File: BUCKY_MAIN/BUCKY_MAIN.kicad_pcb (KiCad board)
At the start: 2 copper layers, 156.4 x 156.4 mm, 43 parts, among them IC1 TSSP96038TR, IC10 TSSP96038TR, IC11 TSSP96038TR, IC12 TSSP96038TR, IC2 TSSP96038TR, IC3 TSSP96038TR, IC4 TSSP96038TR, IC5 TSSP96038TR, IC6 TSSP96038TR, IC7 TSSP96038TR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

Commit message: finish up robot (i think)
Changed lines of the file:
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@@
 		(model "${KICAD8_3DMODEL_DIR}/Connector_PinHeader_2.54mm.3dshapes/PinHeader_1x06_P2.54mm_Horizontal.wrl"
 			(offset
-				(xyz 0 0 0)
+				(xyz 0 -12.75 -2)
 			)
 			(scale
@@
 			)
 			(rotate
-				(xyz 0 0 0)
+				(xyz 180 0 0)
 			)
 		)
@@
 		)
 	)
+	(gr_text "MAIN -> LIGHT\n"
+		(at 167.5638 140.9192 90)
+		(layer "F.SilkS")
+		(effects
+			(font
+				(size 1.5 1.5)
+				(thickness 0.3)
+				(bold yes)
+			)
+			(justify left bottom)
+		)
+	)

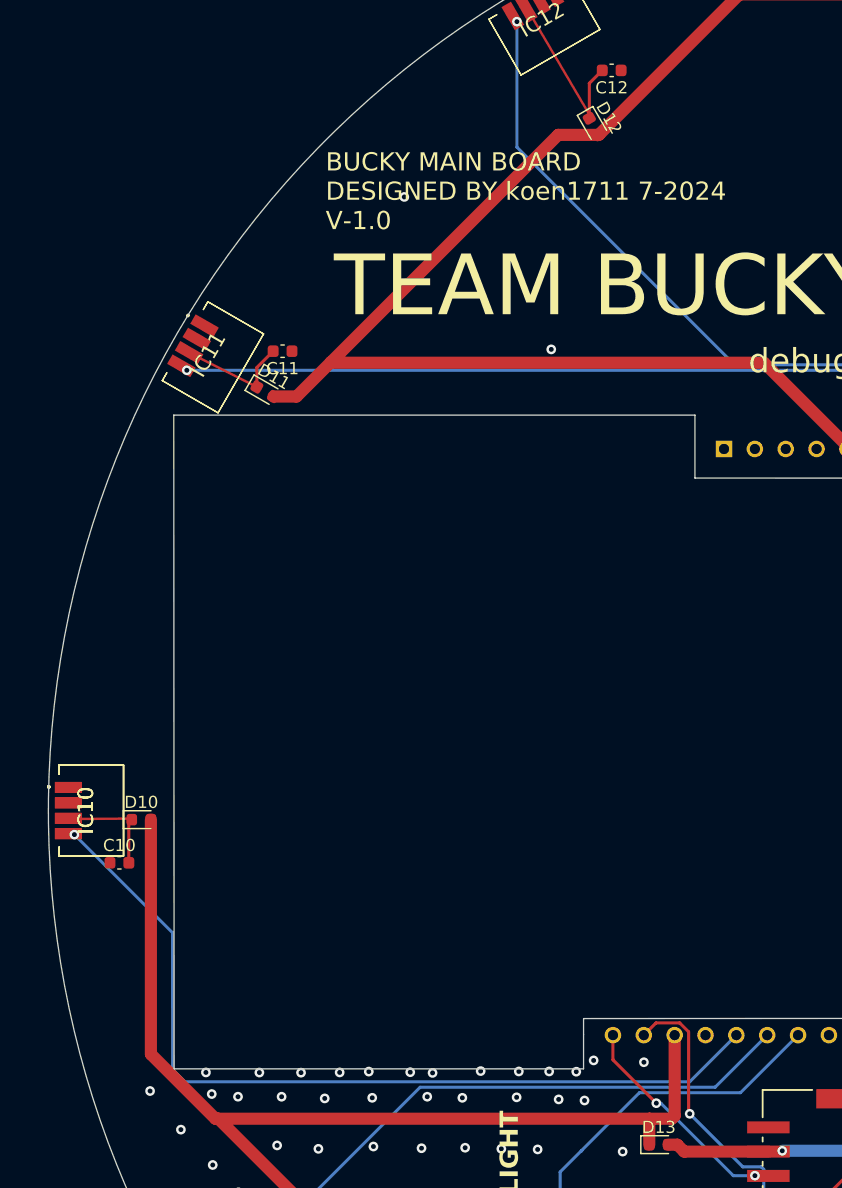
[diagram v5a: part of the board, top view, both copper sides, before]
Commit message: chore: convert 2 layer DRIVE -> 4 layer
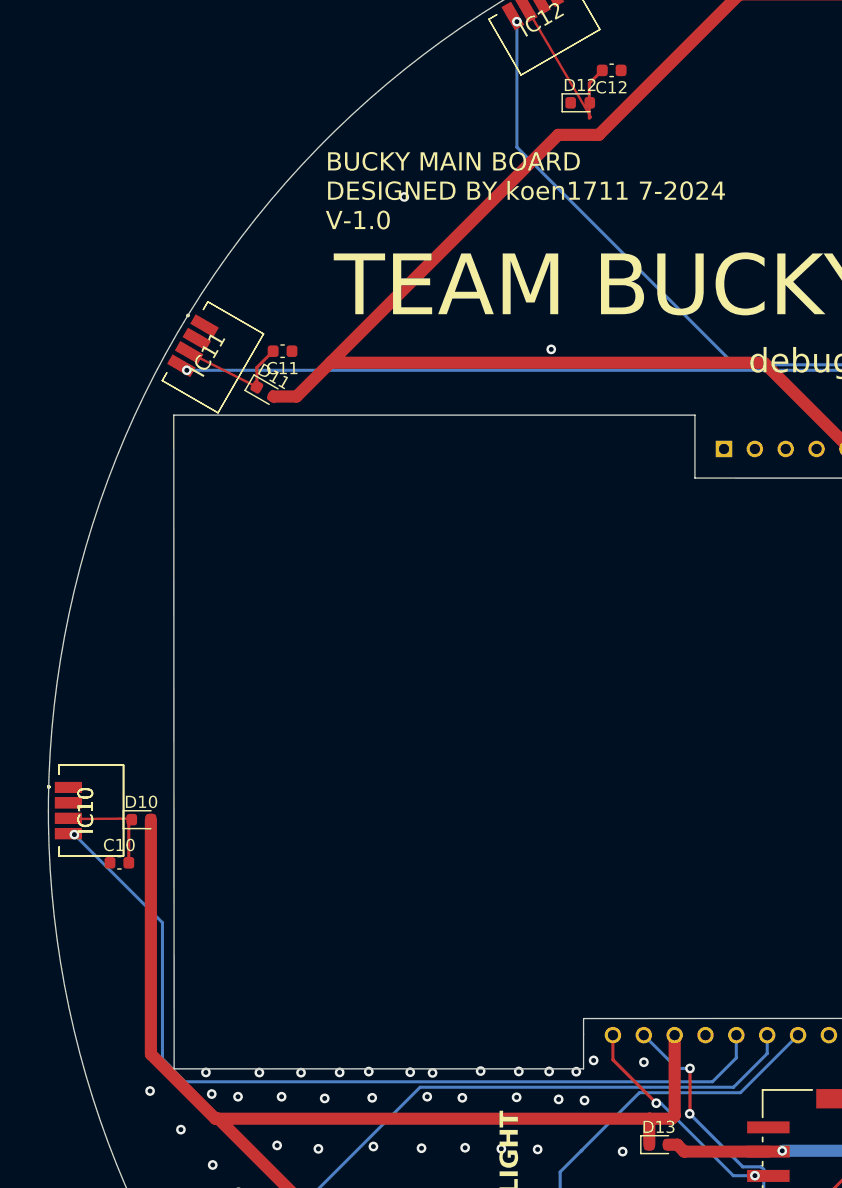
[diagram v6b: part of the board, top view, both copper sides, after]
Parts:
- moved D12 2.27 mm to (86.2, 39.7), turned to 0 degrees
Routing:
- net /SDA: track 22.8 -> 20.3 mm, vias 2 -> 3
- net /IR_10: track 71.1 -> 72.2 mm
- net /IR_9: track 54.3 -> 55.2 mm
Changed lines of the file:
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@@
 	(footprint "Diode_SMD:D_0603_1608Metric"
 		(layer "F.Cu")
-		(at 87.376 41.656 -60)
+		(at 86.233 39.7002)
 		(descr "Diode SMD 0603 (1608 Metric), square (rectangular) end terminal, IPC_7351 nominal, (Body size source: http://www.tortai-tech.com/upload/download/2011102023233369053.pdf), generated with kicad-footprint-generator")
 		(tags "diode")
 		(property "Reference" "D12"
-			(at 0 -1.43 120)
+			(at 0 -1.43 360)
 			(layer "F.SilkS")
 			(effects
@@
 		)
 		(property "Value" "D"
-			(at 0 1.43 120)
+			(at 0 1.43 360)
 			(layer "F.Fab")
 			(effects
@@
 		)
 		(property "Footprint" "Diode_SMD:D_0603_1608Metric"
-			(at 0 0 -60)
+			(at 0 0 0)
 			(unlocked yes)
 			(layer "F.Fab")
@@
 		)
 		(property "Datasheet" ""
-			(at 0 0 -60)
+			(at 0 0 0)
 			(unlocked yes)
 			(layer "F.Fab")
@@
 		)
 		(property "Description" "Diode"
-			(at 0 0 -60)
+			(at 0 0 0)
 			(unlocked yes)
 			(layer "F.Fab")
@@
 		)
 		(property "Sim.Device" "D"
-			(at 0 0 -60)
+			(at 0 0 0)
 			(unlocked yes)
 			(layer "F.Fab")
@@
 		)
 		(property "Sim.Pins" "1=K 2=A"
-			(at 0 0 -60)
+			(at 0 0 0)
 			(unlocked yes)
 			(layer "F.Fab")
@@
 		(attr smd)
 		(fp_line
-			(start -1.485 0.735)
-			(end 0.8 0.735)
+			(start -1.485 -0.735)
+			(end -1.485 0.735)
 			(stroke
 				(width 0.12)
@@
 		)
 		(fp_line
-			(start -1.485 -0.735)
-			(end -1.485 0.735)
+			(start -1.485 0.735)
+			(end 0.8 0.735)
 			(stroke
 				(width 0.12)
@@
 		)
 		(fp_line
-			(start 0.8 0.4)
-			(end 0.8 -0.4)
+			(start -0.5 -0.4)
+			(end -0.799999 -0.1)
 			(stroke
 				(width 0.1)
@@
 		)
 		(fp_line
-			(start -0.5 -0.4)
-			(end -0.799999 -0.1)
+			(start 0.8 -0.4)
+			(end -0.5 -0.4)
 			(stroke
 				(width 0.1)
@@
 		)
 		(fp_line
-			(start 0.8 -0.4)
-			(end -0.5 -0.4)
+			(start 0.8 0.4)
+			(end 0.8 -0.4)
 			(stroke
 				(width 0.1)
@@
 		)
 		(fp_text user "${REFERENCE}"
-			(at 0 0 120)
+			(at 0 0 360)
 			(layer "F.Fab")
 			(effects
@@
 		)
 		(pad "1" smd roundrect
-			(at -0.7875 0 300)
+			(at -0.7875 0)
 			(size 0.875 0.95)
 			(layers "F.Cu" "F.Paste" "F.Mask")
@@
 		)
 		(pad "2" smd roundrect
-			(at 0.7875 0 300)
+			(at 0.7875 0)
 			(size 0.875 0.95)
 			(layers "F.Cu" "F.Paste" "F.Mask")
@@
 	)
 	(segment
-		(start 97.34 120.75)
-		(end 73.052 120.75)
+		(start 73.052 120.75)
+		(end 56.134 137.668)
 		(width 0.25)
 		(layer "B.Cu")
@@
 	)
 	(segment
-		(start 73.052 120.75)
-		(end 56.134 137.668)
+		(start 101.63 116.46)
+		(end 101.63 117.9784)
 		(width 0.25)
 		(layer "B.Cu")
@@
 	)
 	(segment
-		(start 101.63 116.46)
-		(end 97.34 120.75)
+		(start 101.63 117.9784)
+		(end 98.8584 120.75)
+		(width 0.25)
+		(layer "B.Cu")
+		(net 5)
+	)
+	(segment
+		(start 98.8584 120.75)
+		(end 73.052 120.75)
 		(width 0.25)
 		(layer "B.Cu")
@@
 	)
 	(segment
-		(start 52.676476 119.235552)
-		(end 52.669923 108.029923)
+		(start 99.09 116.46)
+		(end 99.09 118.334)
 		(width 0.25)
 		(layer "B.Cu")
@@
 	)
 	(segment
-		(start 53.689699 120.3)
-		(end 52.676476 119.286777)
+		(start 99.09 118.334)
+		(end 97.124 120.3)
 		(width 0.25)
 		(layer "B.Cu")
@@
 	)
 	(segment
-		(start 95.25 120.3)
+		(start 97.124 120.3)
 		(end 53.689699 120.3)
 		(width 0.25)
@@
 	)
 	(segment
-		(start 99.09 116.46)
-		(end 95.25 120.3)
+		(start 51.8414 107.2014)
+		(end 44.59 99.95)
 		(width 0.25)
 		(layer "B.Cu")
@@
 	)
 	(segment
-		(start 52.669923 108.029923)
-		(end 44.59 99.95)
+		(start 51.8414 118.400476)
+		(end 51.8414 107.2014)
+		(width 0.25)
+		(layer "B.Cu")
+		(net 31)
+	)
+	(segment
+		(start 52.676476 119.235552)
+		(end 51.8414 118.400476)
 		(width 0.25)
 		(layer "B.Cu")
@@
 	)
 	(segment
+		(start 53.689699 120.3)
+		(end 52.676476 119.286777)
+		(width 0.25)
+		(layer "B.Cu")
+		(net 31)
+	)
+	(segment
 		(start 49.07 98.9625)
 		(end 49.3125 98.72)
@@
 	)
 	(segment
-		(start 92.476 115.454)
-		(end 91.47 116.46)
-		(width 0.254)
-		(layer "F.Cu")
-		(net 64)
-	)
-	(segment
-		(start 95.25 122.936)
-		(end 95.16 122.846)
-		(width 0.254)
-		(layer "F.Cu")
-		(net 64)
-	)
-	(segment
-		(start 95.16 116.187301)
-		(end 94.426699 115.454)
+		(start 95.2754 119.2022)
+		(end 95.2754 122.9106)
 		(width 0.254)
 		(layer "F.Cu")
@@
 	)
 	(segment
-		(start 95.16 122.846)
-		(end 95.16 116.187301)
-		(width 0.254)
-		(layer "F.Cu")
-		(net 64)
-	)
-	(segment
-		(start 94.426699 115.454)
-		(end 92.476 115.454)
+		(start 95.2754 122.9106)
+		(end 95.25 122.936)
 		(width 0.254)
 		(layer "F.Cu")
@@
 		(net 64)
 	)
+	(via
+		(at 95.2754 119.2022)
+		(size 0.8)
+		(drill 0.4)
+		(layers "F.Cu" "B.Cu")
+		(net 64)
+	)
 	(segment
 		(start 101.141 127.303)
@@
 		(width 0.254)
 		(layer "B.Cu")
+		(net 64)
+	)
+	(segment
+		(start 95.2754 119.2022)
+		(end 94.2122 119.2022)
+		(width 0.254)
+		(layer "B.Cu")
+		(net 64)
+	)
+	(segment
+		(start 94.2122 119.2022)
+		(end 91.47 116.46)
+		(width 0.254)
+		(layer "B.Cu")

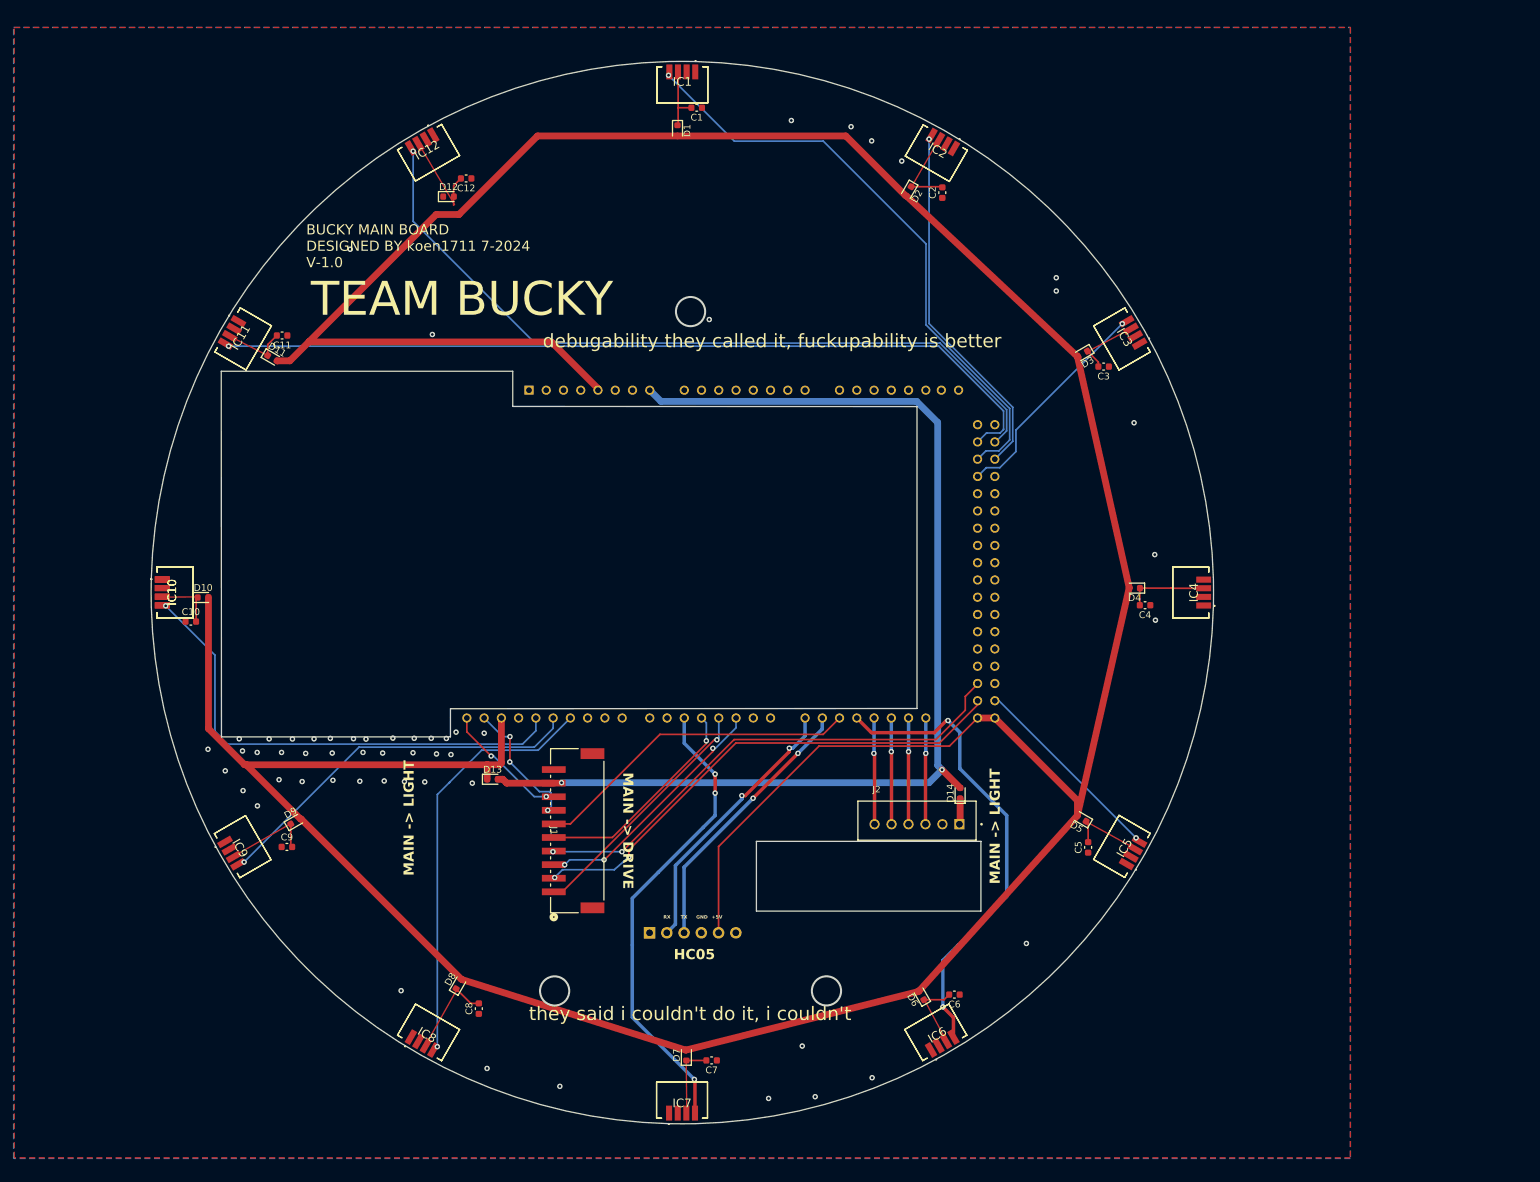
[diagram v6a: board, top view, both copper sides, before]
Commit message: chore: make all PCBs from 2 layers to 4 layers
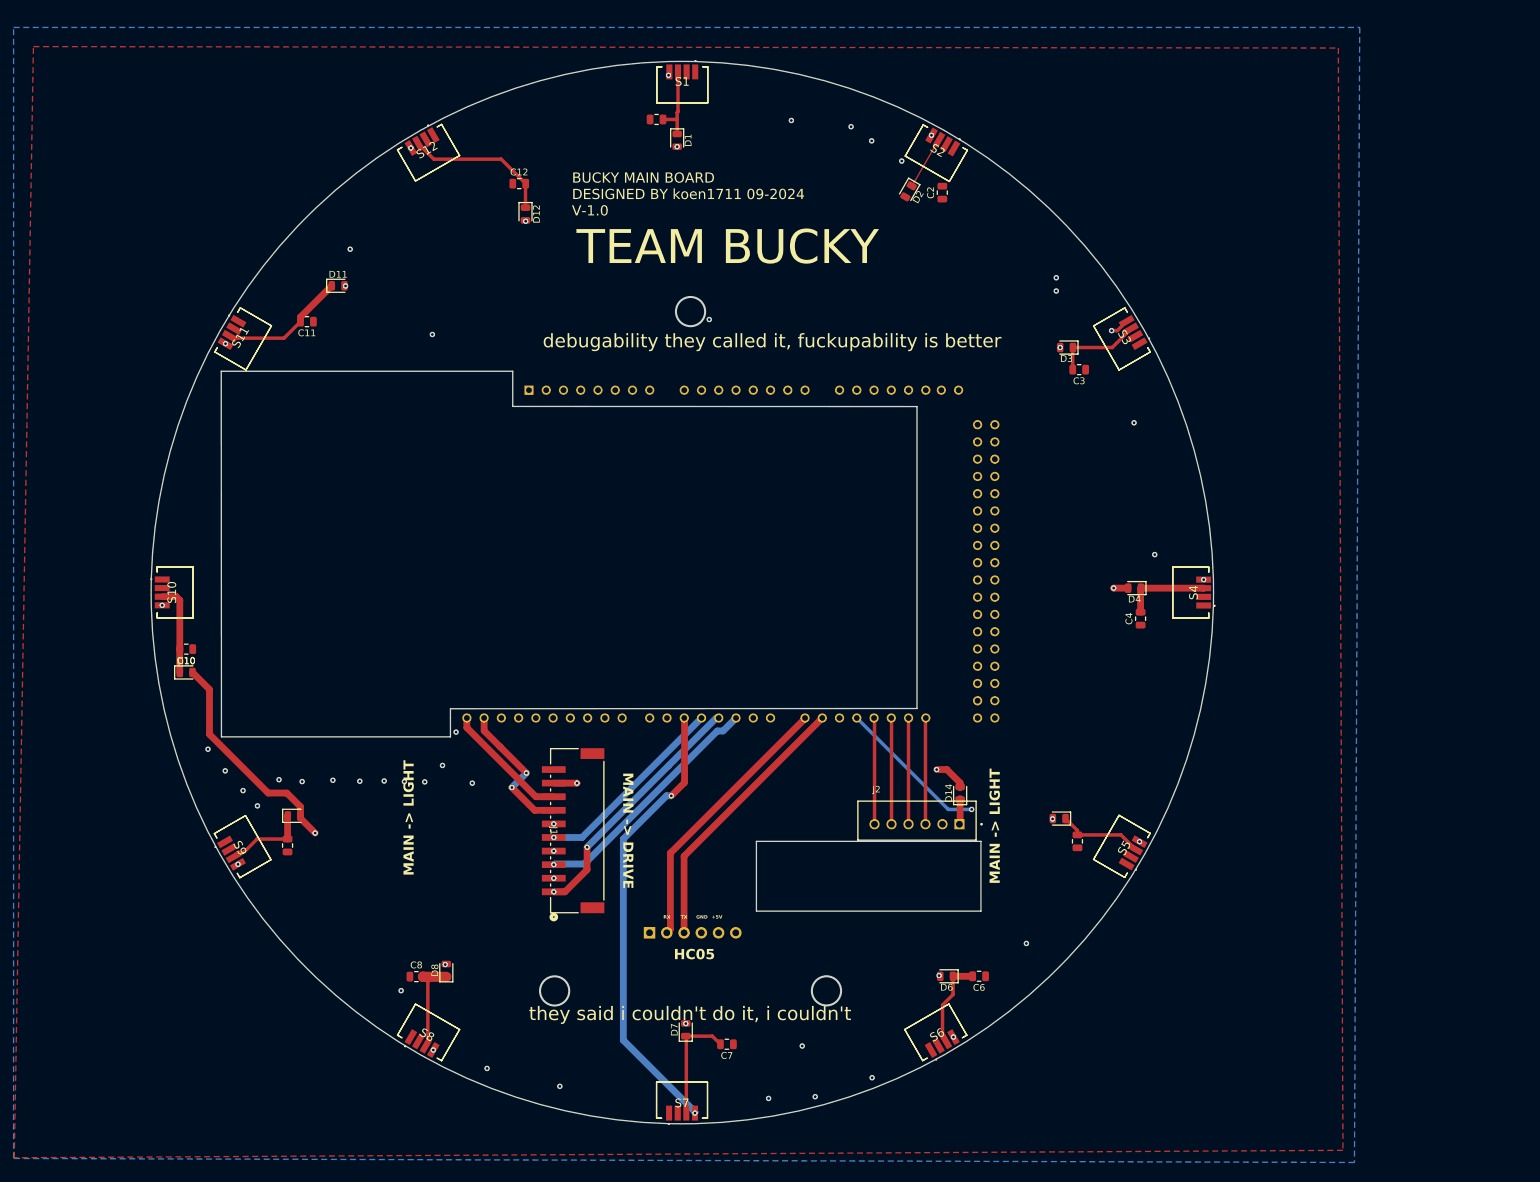
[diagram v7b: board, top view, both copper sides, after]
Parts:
- removed A2: Arduino Mega, BUCKY_MAIN:ARDUINO_MEGA
- removed D13: D, Diode_SMD:D_0603_1608Metric
- removed IC1, IC10 (x2), IC11, IC12, IC2, IC3, IC4, IC5, IC6, IC7, IC8, IC9: TSSP96038TR, BUCKY_MAIN:TSSP96038
- added A1: Arduino Mega, BUCKY_MAIN:ARDUINO_MEGA, B.Cu at (120.9, 92.3)
- added S1: TSSP96038TR, BUCKY_MAIN:TSSP96038, F.Cu at (120.6, 23.2)
- added S10: TSSP96038TR, BUCKY_MAIN:TSSP96038, F.Cu at (46.0, 98.0)
- added S11: TSSP96038TR, BUCKY_MAIN:TSSP96038, F.Cu at (56.0, 60.7)
- added S12: TSSP96038TR, BUCKY_MAIN:TSSP96038, F.Cu at (83.3, 33.2)
- added S2: TSSP96038TR, BUCKY_MAIN:TSSP96038, F.Cu at (158.0, 33.3)
- added S3: TSSP96038TR, BUCKY_MAIN:TSSP96038, F.Cu at (185.4, 60.7)
- added S4: TSSP96038TR, BUCKY_MAIN:TSSP96038, F.Cu at (195.5, 98.0)
- added S5: TSSP96038TR, BUCKY_MAIN:TSSP96038, F.Cu at (185.4, 135.4)
- added S6: TSSP96038TR, BUCKY_MAIN:TSSP96038, F.Cu at (158.0, 162.7)
- added S7: TSSP96038TR, BUCKY_MAIN:TSSP96038, F.Cu at (120.6, 172.7)
- added S8: TSSP96038TR, BUCKY_MAIN:TSSP96038, F.Cu at (83.3, 162.7)
- added S9: TSSP96038TR, BUCKY_MAIN:TSSP96038, F.Cu at (55.9, 135.4)
- C1, C10, C11, C12, C2, C3, C4, C5, C6, C7, C8, C9: footprint Capacitor_SMD:C_0603_1608Metric -> Capacitor_SMD:C_0805_2012Metric
- D1, D10, D11, D12, D14, D2, D3, D4, D5, D6, D7, D8, D9: footprint Diode_SMD:D_0603_1608Metric -> Diode_SMD:D_0805_2012Metric
- moved D11 14.4 mm to (70.0, 52.8), turned to 0 degrees
- moved D12 11.6 mm to (97.6, 42.3), turned to -90 degrees
- moved D10 11.3 mm to (47.6, 109.8)
- moved C8 10.3 mm to (81.5, 154.5), turned to 0 degrees
- moved C12 7.85 mm to (96.6, 37.8), turned to 0 degrees
- moved C1 6.16 mm to (116.9, 28.3), turned to 0 degrees
- moved D6 4.65 mm to (159.6, 154.5), turned to 180 degrees
- moved C6 4.52 mm to (164.3, 154.5)
- moved C11 4.19 mm to (65.4, 58.1)
- moved C10 4.11 mm to (47.6, 106.3), turned to 180 degrees
- moved D7 3.73 mm to (121.2, 162.4)
- moved C3 3.63 mm to (179.1, 65.2)
- moved C7 3.28 mm to (127.2, 164.5)
- moved D5 3.28 mm to (176.1, 131.3), turned to 180 degrees
- moved D8 2.72 mm to (85.9, 153.6), turned to 90 degrees
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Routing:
- net +5V: track 321.0 -> 461.2 mm, vias 0 -> 10
- net /IR_4: track 0.00 -> 33.9 mm, vias 0 -> 1
- net Net-(D12-K): track 4.39 -> 21.8 mm
- net Net-(D11-K): track 3.50 -> 18.7 mm
- net /IR_11: track 125.4 -> 139.9 mm
- net Net-(D7-K): track 2.95 -> 17.0 mm
- net Net-(D3-K): track 2.95 -> 13.0 mm
- net Net-(D8-K): track 4.24 -> 14.1 mm
- net Net-(D10-K): track 3.65 -> 13.4 mm
- net /IR_6: track 69.8 -> 60.4 mm
- net Net-(D6-K): track 4.03 -> 13.3 mm
- net Net-(D5-K): track 3.23 -> 12.5 mm
- net Net-(D9-K): track 3.46 -> 12.5 mm
- net /IR_3: track 32.5 -> 40.2 mm
- net Net-(D2-K): track 4.62 -> 0.00 mm
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- added copper zone on In1.Cu, net GND
- added copper zone on In2.Cu, net GND
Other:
- copper layers 2 -> 4
- board text added: "BUCKY MAIN BOARD DESIGNED BY koen1711 09-2024 V-1.0"
- board text removed: "BUCKY MAIN BOARD DESIGNED BY koen1711 7-2024 V-1.0"

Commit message: fix all drc issues
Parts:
- moved D14 3.64 mm to (160.6, 124.0), turned to 180 degrees
- moved C2 1.73 mm to (158.5, 40.8)
- moved D2 1.26 mm to (153.9, 40.2), turned to -90 degrees
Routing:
- net Net-(D2-K): track 0.00 -> 14.7 mm
- net Net-(D14-K): track 3.68 -> 7.98 mm
- net /VIN: track 169.6 -> 166.2 mm
- net +5V: track 461.2 -> 464.3 mm, vias 10 -> 11
- net /M2_PWM: vias 2 -> 1
